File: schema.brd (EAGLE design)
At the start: 40 x 70 mm, 9 parts

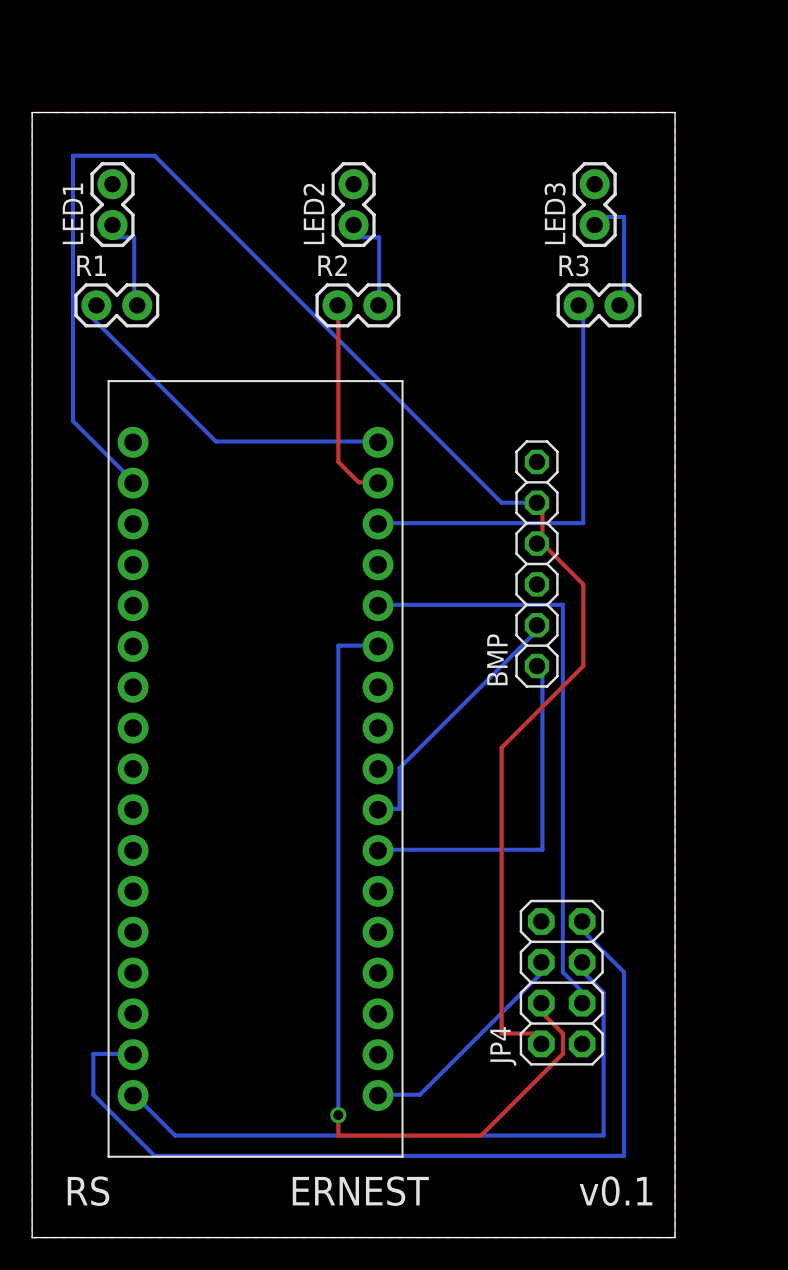
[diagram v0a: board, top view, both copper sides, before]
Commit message: ERNEST v0.2
Added a DIP switch for quick setting of the node ID, to avoid
having to reflash the thing each time.
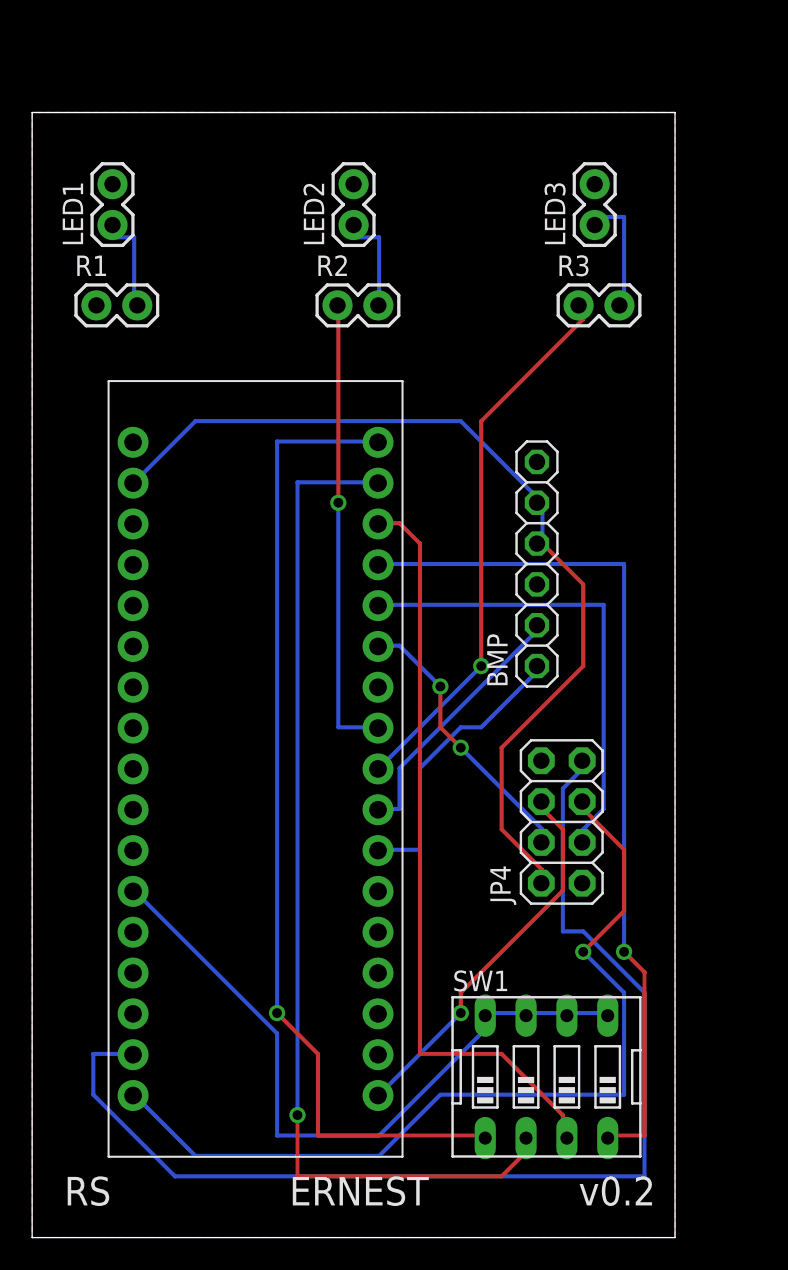
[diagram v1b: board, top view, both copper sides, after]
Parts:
- added SW1: (no value), special:EDG-04
- moved JP4 10.0 mm to (33.0, 25.9)
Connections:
- new net N$1: R3.1, U$1.P$9
- new net N$14: SW1.2, U$1.P$2
- new net N$15: SW1.3, U$1.P$3
- new net N$16: SW1.4, U$1.P$4
- new net N$8: R2.1, U$1.P$8
- net N$11: now also U$1.P$7; no longer R3.1, U$1.P$3
- net N$12: now also SW1.5, SW1.6, SW1.7, SW1.8, U$1.P$23; no longer R2.1, U$1.P$2
- net N$13: now also SW1.1; no longer R1.1
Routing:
- net N$14: track 0.00 -> 64.0 mm, vias 0 -> 1
- net N$16: track 0.00 -> 54.2 mm, vias 0 -> 1
- net N$15: track 0.00 -> 46.9 mm
- net VCC: track 100.2 -> 58.1 mm
- net N$13: track 21.9 -> 61.1 mm, vias 0 -> 1
- net N$3: track 52.9 -> 17.3 mm, vias 1 -> 2
- net N$1: track 0.00 -> 34.2 mm, vias 0 -> 1
- net N$12: track 12.9 -> 44.3 mm
- net N$8: track 0.00 -> 28.9 mm, vias 0 -> 1
- net N$11: track 26.4 -> 0.00 mm
- net N$10: track 55.4 -> 70.8 mm
- net N$7: track 41.7 -> 55.1 mm, vias 0 -> 1
- net N$9: track 14.0 -> 23.6 mm, vias 0 -> 1
- net N$2: track 36.8 -> 29.4 mm
- net SDA: track 22.0 -> 18.3 mm
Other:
- board text added: "v0.2"
- board text removed: "v0.1"

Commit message: Add mounting holes
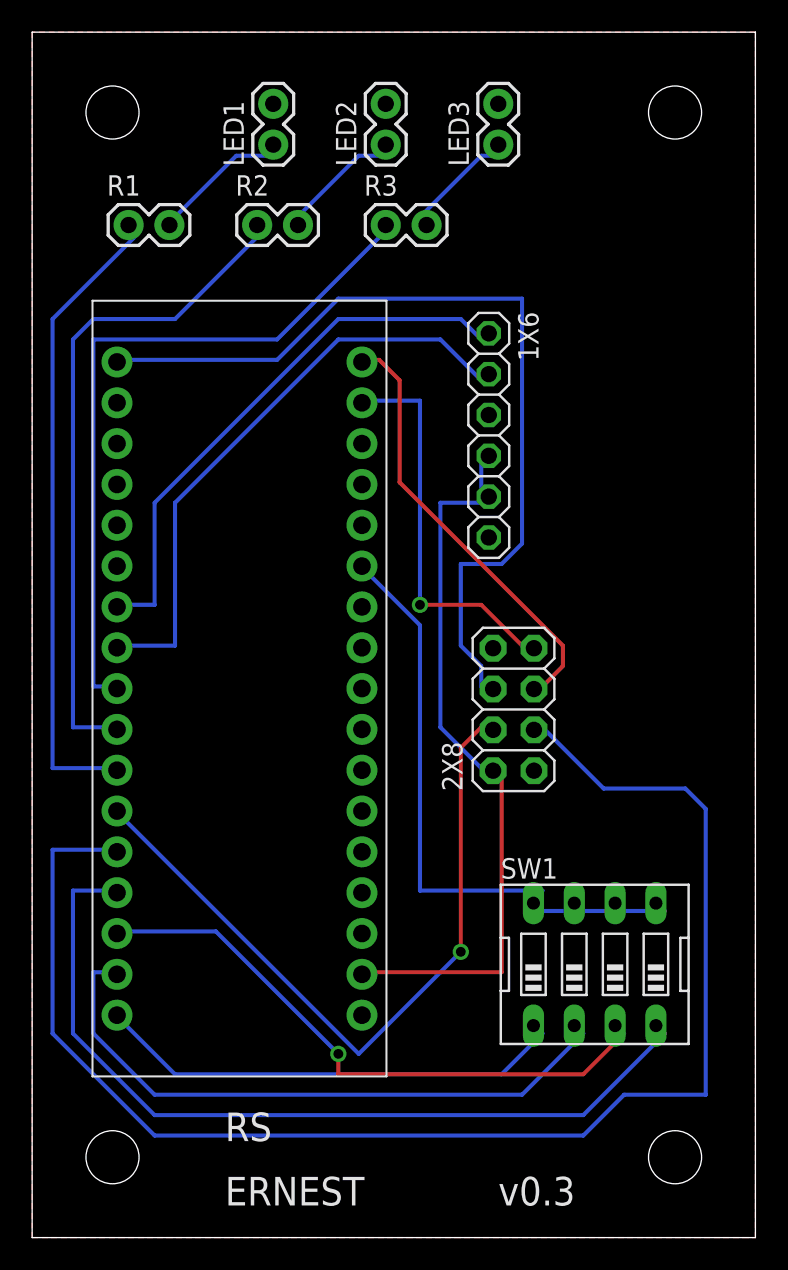
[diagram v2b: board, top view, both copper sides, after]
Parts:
- removed BMP: (no value), adafruit:1X06
- removed JP4: (no value), adafruit:2X04
- added 1X6: BMP180, adafruit:1X06
- added 2X8: 2.4GHz, adafruit:2X04
- added STANDOFF1, STANDOFF2, STANDOFF3, STANDOFF4: STAND-OFF, SparkFun-Electromechanical:STAND-OFF
- SW1: value (none) -> IDENT
- moved R3 13.0 mm to (22.0, 63.0)
- moved LED1 11.2 mm to (15.0, 68.0)
- moved LED3 7.81 mm to (29.0, 68.0)
- moved SW1 7.62 mm to (35.0, 17.0)
- moved R2 7.07 mm to (14.0, 63.0)
- moved LED2 5.39 mm to (22.0, 68.0)
- moved R1 5.39 mm to (6.00, 63.0)
- moved U$1 5.10 mm to (12.9, 34.2), turned to 90 degrees
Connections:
- net GND: now also 1X6.3, 2X8.1; no longer BMP.3, JP4.1
- net N$10: now also 2X8.7; no longer JP4.7
- net N$11: now also R1.1
- net N$2: now also 2X8.3; no longer JP4.3
- net N$3: now also 2X8.4; no longer JP4.4
- net N$7: now also 2X8.5; no longer JP4.5
- net N$9: now also 2X8.6; no longer JP4.6
- net SCL: now also 1X6.2; no longer BMP.2
- net SDA: now also 1X6.1; no longer BMP.1
- net VCC: now also 1X6.4, 1X6.5, 2X8.2; no longer BMP.4, BMP.5, JP4.2
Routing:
- net N$2: track 29.4 -> 90.4 mm
- net N$10: track 70.8 -> 24.9 mm, vias 0 -> 1
- net N$11: track 0.00 -> 40.0 mm
- net N$9: track 23.6 -> 55.7 mm, vias 1 -> 0
- net N$13: track 61.1 -> 30.3 mm, vias 1 -> 0
- net N$3: track 17.3 -> 46.0 mm, vias 2 -> 1
- net N$7: track 55.1 -> 27.6 mm, vias 1 -> 0
- net N$14: track 64.0 -> 39.7 mm, vias 1 -> 0
- net SCL: track 16.8 -> 37.9 mm
- net SDA: track 18.3 -> 35.3 mm
- net N$8: track 28.9 -> 41.7 mm, vias 1 -> 0
- net VCC: track 58.1 -> 47.0 mm
- net N$1: track 34.2 -> 44.4 mm, vias 1 -> 0
- net N$15: track 46.9 -> 38.2 mm, vias 0 -> 1
- net N$12: track 44.3 -> 41.3 mm
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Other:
- board size 40 x 70 mm -> 45 x 75 mm
- board text added: "v0.3"
- board text removed: "v0.2"
